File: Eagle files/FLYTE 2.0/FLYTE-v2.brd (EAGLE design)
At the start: 116 x 55 mm, 56 parts, among them U2 XBP9B-XCST-021, U3 ADS1115IDGSR, U4 H3LIS200DLTR, U5 BS170F, U6 W25Q32JVSSIQ, U7 BS170F

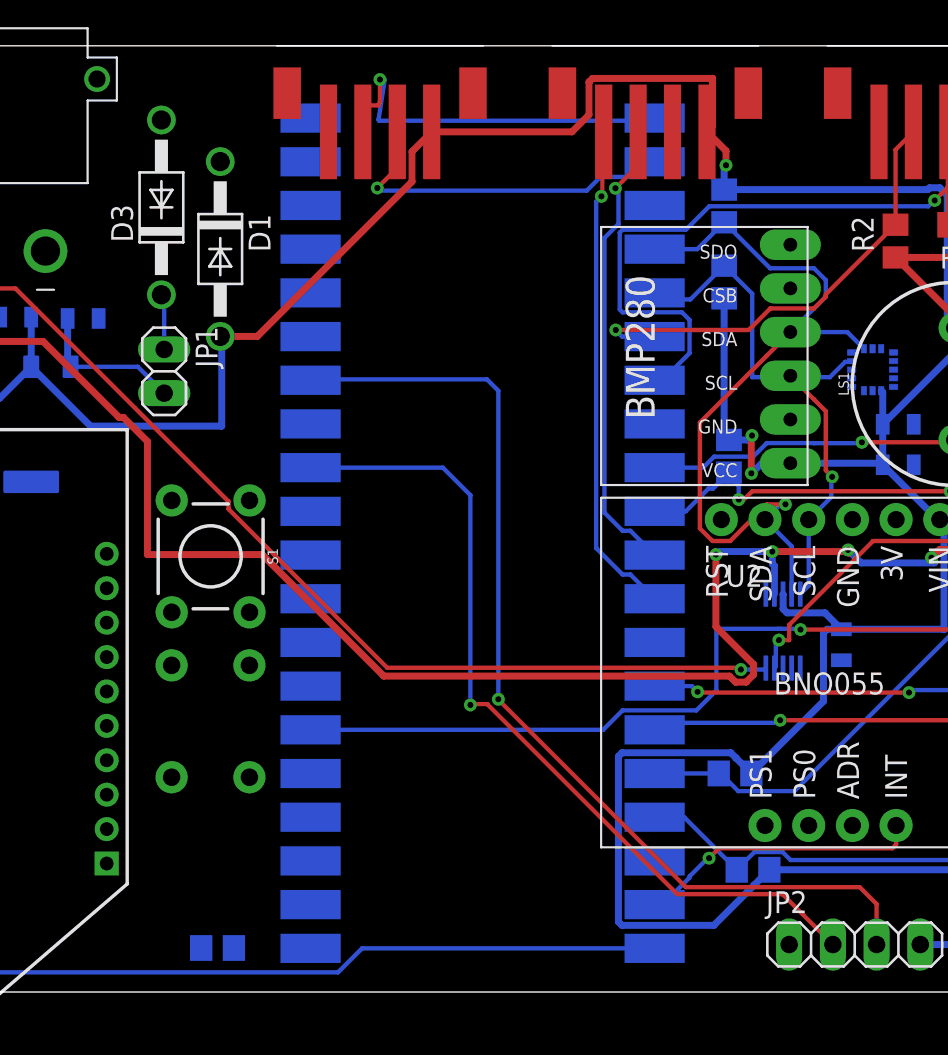
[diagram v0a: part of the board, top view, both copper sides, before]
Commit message: layout done. drc left to clear
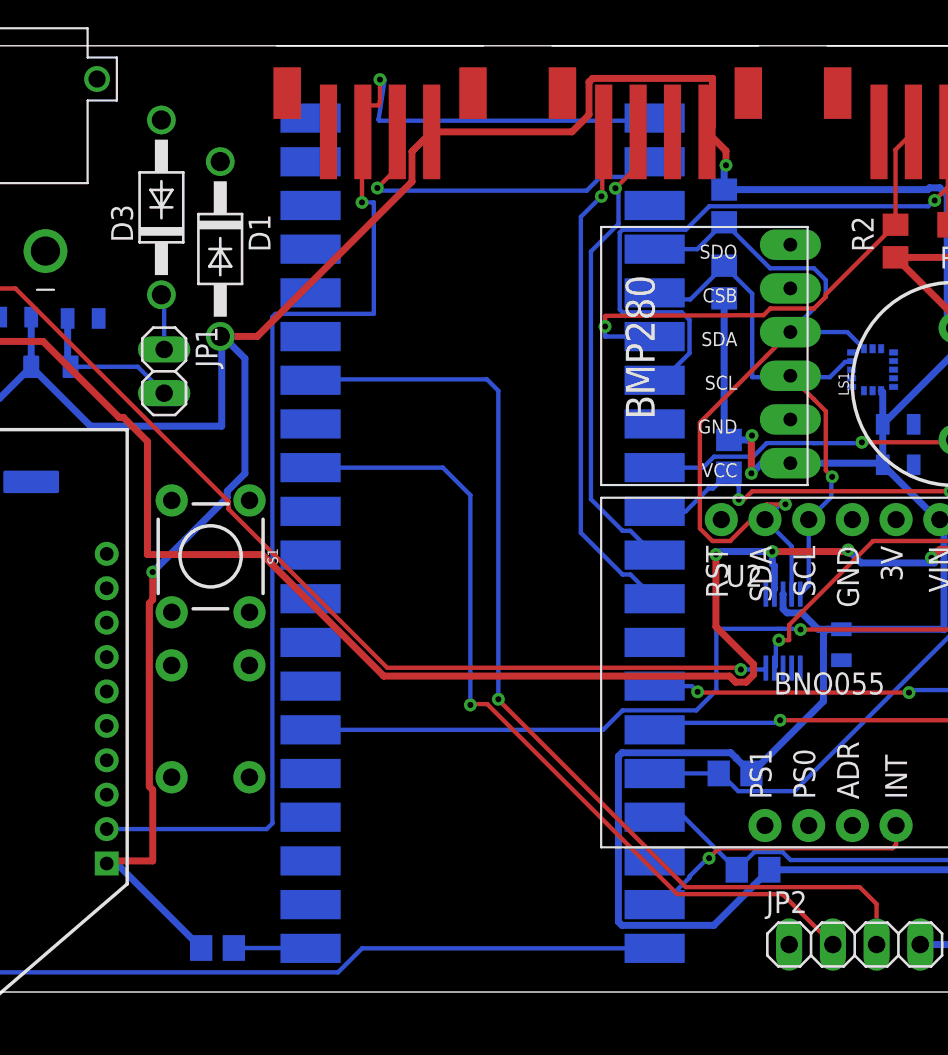
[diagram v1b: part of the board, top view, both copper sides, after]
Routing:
- net SER_TX: track 22.8 -> 79.4 mm, vias 1 -> 2
- net 3V3: track 266.3 -> 310.0 mm, vias 4 -> 5
- net MISO0: track 0.00 -> 4.47 mm
- net SDA0: track 27.2 -> 29.0 mm
- net RX: track 29.0 -> 29.7 mm
- net TX: track 27.3 -> 27.9 mm
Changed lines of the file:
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@@
 <wire x1="18" y1="50.73" x2="22.5998" y2="50.73" width="0.4064" layer="16"/>
 <wire x1="22.5998" y1="50.73" x2="30.4049" y2="42.9249" width="0.4064" layer="16"/>
-<wire x1="77.9224" y1="23.129" x2="77.9224" y2="24.7698" width="0.4064" layer="16"/>
 <via x="77.8002" y="25.6032" extent="1-16" drill="0.35"/>
 <wire x1="77.8002" y1="25.6032" x2="82.169" y2="25.6032" width="0.4064" layer="1"/>
@@
 <wire x1="98" y1="37.06175" x2="98" y2="50.73" width="0.4064" layer="1"/>
 <wire x1="94.059" y1="33.12075" x2="98" y2="37.06175" width="0.4064" layer="1"/>
-<wire x1="77.9224" y1="24.7698" x2="77.8002" y2="24.892" width="0.4064" layer="16"/>
+<wire x1="77.8002" y1="24.892" x2="77.9224" y2="24.7698" width="0.4064" layer="16"/>
 <wire x1="77.8002" y1="24.892" x2="77.8002" y2="25.6032" width="0.4064" layer="16"/>
 <wire x1="77.8002" y1="25.6032" x2="74.5236" y2="25.6032" width="0.4064" layer="16"/>
@@
 <wire x1="41.4782" y1="32.004" x2="41.4782" y2="25.4254" width="0.4064" layer="1"/>
 <wire x1="35.4076" y1="37.8206" x2="39.8272" y2="33.401" width="0.4064" layer="1"/>
+<wire x1="77.9224" y1="24.7698" x2="77.9224" y2="23.41926875" width="0.4064" layer="16"/>
+<wire x1="77.9224" y1="23.41926875" x2="77.918" y2="23.41486875" width="0.4064" layer="16"/>
+<wire x1="77.918" y1="23.41486875" x2="77.9224" y2="23.129" width="0" layer="19" extent="16-16"/>
 </signal>
 <signal name="SCL1">
@@
 <wire x1="84.9614" y1="42.7042" x2="88.347" y2="39.3186" width="0.4064" layer="1"/>
 <wire x1="88.347" y1="39.3186" x2="88.347" y2="38.5992" width="0.4064" layer="1"/>
-<wire x1="78.65560625" y1="22.0384" x2="78.4268" y2="22.26720625" width="0.4064" layer="16"/>
-<wire x1="81.8148" y1="21.0862" x2="80.8626" y2="22.0384" width="0.4064" layer="16"/>
-<wire x1="78.4268" y1="22.26720625" x2="78.4268" y2="23.1246" width="0.4064" layer="16"/>
-<wire x1="78.4268" y1="23.1246" x2="78.4224" y2="23.129" width="0.4064" layer="16"/>
-<wire x1="80.8626" y1="22.0384" x2="78.65560625" y2="22.0384" width="0.4064" layer="16"/>
 <wire x1="86.4" y1="2.76" x2="95.8764" y2="2.76" width="0.4064" layer="16"/>
 <wire x1="95.8764" y1="2.76" x2="96.98" y2="3.8636" width="0.4064" layer="16"/>
@@
 <wire x1="74.40109375" y1="3.8744" x2="69.06270625" y2="3.8744" width="0.4064" layer="16"/>
 <wire x1="68.8544" y1="4.08270625" x2="68.8544" y2="13.69729375" width="0.4064" layer="16"/>
+<wire x1="39.11" y1="7.47" x2="39.6884" y2="7.47" width="0.4064" layer="16"/>
+<wire x1="39.6884" y1="7.47" x2="44.6008" y2="2.5576" width="0.4064" layer="16"/>
+<wire x1="39.11" y1="7.47" x2="39.26" y2="7.62" width="0.4064" layer="1"/>
+<wire x1="39.26" y1="7.62" x2="41.783" y2="7.62" width="0.4064" layer="1"/>
+<wire x1="41.783" y1="7.62" x2="41.783" y2="11.753425" width="0.4064" layer="1"/>
+<wire x1="41.783" y1="11.753425" x2="41.5874" y2="11.949025" width="0.4064" layer="1"/>
+<wire x1="41.5874" y1="11.949025" x2="41.5874" y2="22.602375" width="0.4064" layer="1"/>
+<wire x1="41.5874" y1="22.602375" x2="41.783" y2="22.797975" width="0.4064" layer="1"/>
+<via x="41.783" y="24.4094" extent="1-16" drill="0.35"/>
+<wire x1="41.783" y1="24.4094" x2="46.115" y2="28.7414" width="0.4064" layer="16"/>
+<wire x1="46.115" y1="28.7414" x2="46.115" y2="29.111175" width="0.4064" layer="16"/>
+<wire x1="47.1424" y1="30.138575" x2="47.1424" y2="36.83" width="0.4064" layer="16"/>
+<wire x1="46.115" y1="29.111175" x2="47.1424" y2="30.138575" width="0.4064" layer="16"/>
+<wire x1="47.1424" y1="36.83" x2="45.9486" y2="38.0238" width="0.4064" layer="16"/>
+<wire x1="45.9486" y1="38.0238" x2="45.7962" y2="38.0238" width="0.4064" layer="16"/>
+<wire x1="41.783" y1="22.797975" x2="41.783" y2="24.4094" width="0.4064" layer="1"/>
+<wire x1="80.4652" y1="21.0862" x2="81.8148" y2="21.0862" width="0.4064" layer="16"/>
+<wire x1="78.4224" y1="23.129" x2="78.4268" y2="23.1246" width="0.4064" layer="16"/>
+<wire x1="78.4268" y1="23.1246" x2="78.4268" y2="22.26720625" width="0.4064" layer="16"/>
+<wire x1="78.4268" y1="22.26720625" x2="78.65560625" y2="22.0384" width="0.4064" layer="16"/>
+<wire x1="79.513" y1="22.0384" x2="80.4652" y2="21.0862" width="0.4064" layer="16"/>
+<wire x1="78.65560625" y1="22.0384" x2="79.513" y2="22.0384" width="0.4064" layer="16"/>
 <wire x1="83.6266" y1="34.955" x2="82.4066" y2="35.175" width="0" layer="19" extent="16-16"/>
 <wire x1="84.1266" y1="34.955" x2="83.6266" y2="34.955" width="0" layer="19" extent="16-16"/>
 <wire x1="77.4224" y1="23.129" x2="78.4224" y2="23.129" width="0" layer="19" extent="16-16"/>
-<wire x1="39.11" y1="7.47" x2="34.72" y2="36.345" width="0" layer="19" extent="16-16"/>
-<wire x1="44.6008" y1="2.5576" x2="39.11" y2="7.47" width="0" layer="19" extent="16-16"/>
 </signal>
 <signal name="TX">
@@
 <wire x1="70.96" y1="25.4" x2="69.5494" y2="26.8106" width="0.254" layer="16"/>
 <wire x1="69.5494" y1="26.8106" x2="69.09426875" y2="26.8106" width="0.254" layer="16"/>
-<wire x1="68.0416" y1="43.83146875" x2="68.8594" y2="44.64926875" width="0.254" layer="16"/>
+<wire x1="67.2542" y1="43.04406875" x2="68.8594" y2="44.64926875" width="0.254" layer="16"/>
 <wire x1="68.8594" y1="44.64926875" x2="68.8594" y2="46.8122" width="0.254" layer="16"/>
-<wire x1="69.09426875" y1="26.8106" x2="68.0416" y2="27.86326875" width="0.254" layer="16"/>
-<wire x1="68.0416" y1="27.86326875" x2="68.0416" y2="43.83146875" width="0.254" layer="16"/>
+<wire x1="69.09426875" y1="26.8106" x2="67.2542" y2="28.65066875" width="0.254" layer="16"/>
+<wire x1="67.2542" y1="28.65066875" x2="67.2542" y2="43.04406875" width="0.254" layer="16"/>
 <wire x1="68.8594" y1="46.8122" x2="68.7722" y2="46.8122" width="0.254" layer="16"/>
 <wire x1="68.7722" y1="46.8122" x2="68.6794" y2="46.7194" width="0.254" layer="16"/>
@@
 <wire x1="70.96" y1="22.86" x2="69.5494" y2="24.2706" width="0.254" layer="16"/>
 <wire x1="69.5494" y1="24.2706" x2="69.09426875" y2="24.2706" width="0.254" layer="16"/>
-<wire x1="69.09426875" y1="24.2706" x2="67.55968125" y2="25.8051875" width="0.254" layer="16"/>
-<wire x1="67.55968125" y1="45.94428125" x2="67.55968125" y2="25.8051875" width="0.254" layer="16"/>
-<wire x1="67.55968125" y1="45.94428125" x2="67.86448125" y2="46.24908125" width="0.254" layer="16"/>
+<wire x1="69.09426875" y1="24.2706" x2="66.67068125" y2="26.6941875" width="0.254" layer="16"/>
+<wire x1="66.67068125" y1="45.05528125" x2="66.67068125" y2="26.6941875" width="0.254" layer="16"/>
+<wire x1="66.67068125" y1="45.05528125" x2="67.86448125" y2="46.24908125" width="0.254" layer="16"/>
 <via x="67.86448125" y="46.24908125" extent="1-16" drill="0.35"/>
 <wire x1="67.86448125" y1="46.24908125" x2="67.9196" y2="46.3042" width="0.254" layer="1"/>
@@
 <contactref element="U1" pad="P$21"/>
 <contactref element="R16" pad="1"/>
-<wire x1="46.5008" y1="2.5576" x2="50.96" y2="2.54" width="0" layer="19" extent="16-16"/>
+<wire x1="46.5008" y1="2.5576" x2="50.9424" y2="2.5576" width="0.254" layer="16"/>
+<wire x1="50.9424" y1="2.5576" x2="50.96" y2="2.54" width="0.254" layer="16"/>
 </signal>
 <signal name="CS_FLASH">
@@
 <wire x1="86" y1="50" x2="84.9614" y2="48.9614" width="0.254" layer="1"/>
 <wire x1="84.9614" y1="48.9614" x2="84.9614" y2="44.6042" width="0.254" layer="1"/>
-<wire x1="70.96" y1="38.1" x2="69.0626" y2="38.1" width="0.254" layer="16"/>
-<wire x1="69.0626" y1="38.1" x2="68.6816" y2="38.481" width="0.254" layer="16"/>
-<wire x1="68.6816" y1="38.481" x2="68.6992" y2="38.481" width="0.254" layer="16"/>
-<via x="68.6992" y="38.481" extent="1-16" drill="0.35"/>
+<wire x1="70.96" y1="38.1" x2="68.0798" y2="38.1" width="0.254" layer="16"/>
+<wire x1="68.0798" y1="38.1" x2="68.0798" y2="38.6842" width="0.254" layer="16"/>
+<via x="68.0798" y="38.6842" extent="1-16" drill="0.35"/>
 <wire x1="80.22296875" y1="39.7316" x2="80.9074" y2="40.41603125" width="0.254" layer="1"/>
 <wire x1="80.9074" y1="40.41603125" x2="80.9074" y2="40.5502" width="0.254" layer="1"/>
 <wire x1="80.9074" y1="40.5502" x2="84.9614" y2="44.6042" width="0.254" layer="1"/>
-<wire x1="68.6992" y1="38.481" x2="76.42963125" y2="38.481" width="0.254" layer="1"/>
-<wire x1="76.42963125" y1="38.481" x2="77.68023125" y2="39.7316" width="0.254" layer="1"/>
+<wire x1="68.11175" y1="39.30596875" x2="68.0798" y2="39.27401875" width="0.254" layer="1"/>
+<wire x1="68.0798" y1="38.6842" x2="68.0798" y2="39.27401875" width="0.254" layer="1"/>
+<wire x1="77.28936875" y1="39.3407375" x2="68.11175" y2="39.30596875" width="0.254" layer="1"/>
+<wire x1="77.28936875" y1="39.3407375" x2="77.68023125" y2="39.7316" width="0.254" layer="1"/>
 <wire x1="77.68023125" y1="39.7316" x2="80.22296875" y2="39.7316" width="0.254" layer="1"/>
 </signal>
@@
 <wire x1="54.991" y1="51.774284375" x2="54.915253125" y2="51.5366" width="0.254" layer="1"/>
 <wire x1="54.915253125" y1="51.5366" x2="54" y2="51.5366" width="0.254" layer="1"/>
-<wire x1="54" y1="51.5366" x2="54" y2="50" width="0.254" layer="1"/>
+<wire x1="54" y1="51.5366" x2="54" y2="50.1904" width="0.254" layer="1"/>
 <contactref element="U2" pad="2"/>
-<wire x1="39.11" y1="9.47" x2="54" y2="50" width="0" layer="19" extent="1-1"/>
+<wire x1="54" y1="50.1904" x2="54" y2="50" width="0.254" layer="1"/>
+<wire x1="39.11" y1="9.47" x2="48.4082" y2="9.47" width="0.254" layer="16"/>
+<wire x1="48.7426" y1="9.8044" x2="48.7426" y2="39.243" width="0.254" layer="16"/>
+<wire x1="48.7426" y1="39.243" x2="48.9204" y2="39.4208" width="0.254" layer="16"/>
+<wire x1="48.9204" y1="39.4208" x2="54.6354" y2="39.4208" width="0.254" layer="16"/>
+<wire x1="54.6354" y1="39.4208" x2="54.6354" y2="45.8978" width="0.254" layer="16"/>
+<wire x1="54.6354" y1="45.8978" x2="53.9496" y2="45.8978" width="0.254" layer="16"/>
+<via x="53.9496" y="45.8978" extent="1-16" drill="0.35"/>
+<wire x1="53.9496" y1="45.8978" x2="53.9496" y2="50.14" width="0.254" layer="1"/>
+<wire x1="53.9496" y1="50.14" x2="54" y2="50.1904" width="0.254" layer="1"/>
+<wire x1="48.4082" y1="9.47" x2="48.7426" y2="9.8044" width="0.254" layer="16"/>
 </signal>
 <signal name="SER_RX">

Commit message: updated layout
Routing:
- net GND: track 0.00 -> 125.5 mm, vias 0 -> 11
- net N$3: track 0.00 -> 23.1 mm, vias 0 -> 1
- net N$8: track 0.00 -> 9.52 mm, vias 0 -> 1
- net N$17: track 0.00 -> 8.72 mm
- net N$1: track 0.00 -> 5.25 mm
- net 3V3: track 310.0 -> 314.7 mm
- net N$5: track 10.4 -> 13.8 mm
- net BNO_INT: track 16.6 -> 19.3 mm
- net N$12: track 7.01 -> 9.18 mm

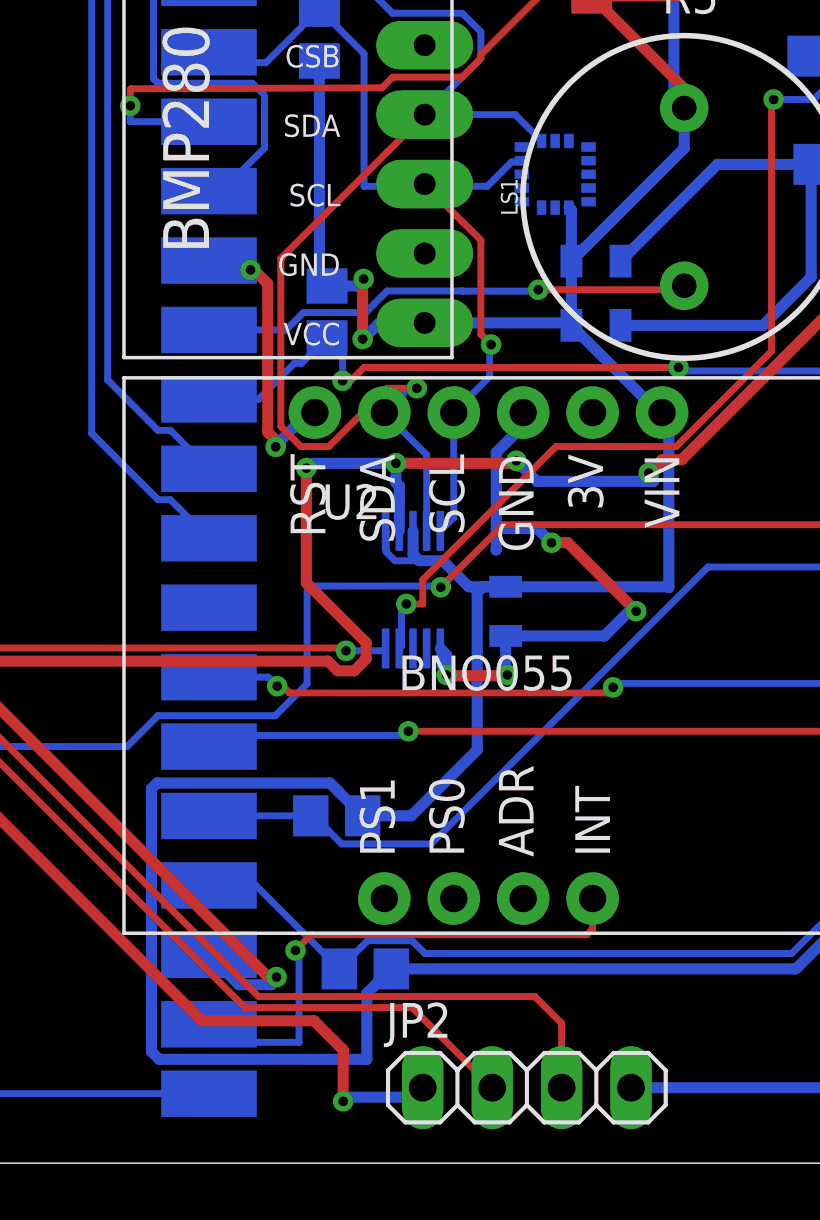
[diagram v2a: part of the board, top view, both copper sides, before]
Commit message: updated layout
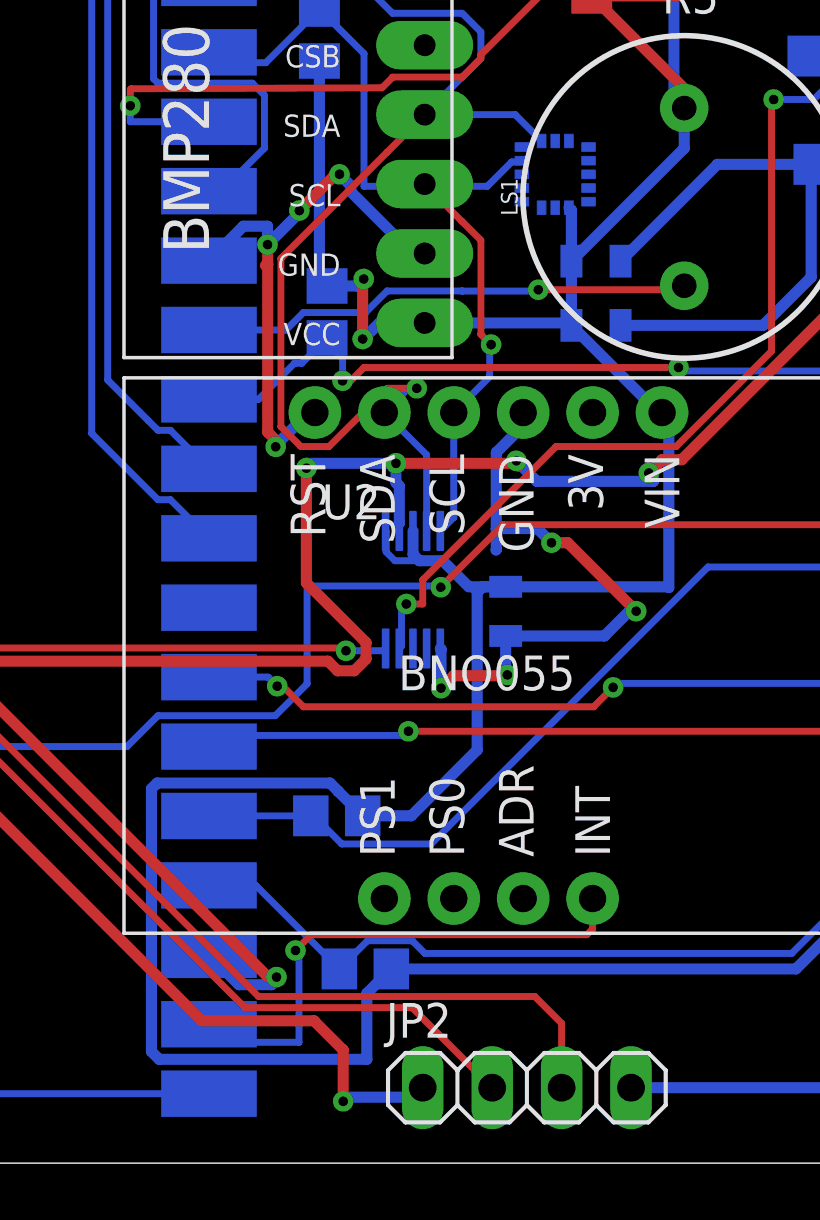
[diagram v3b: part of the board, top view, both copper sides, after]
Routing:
- net GND: track 125.5 -> 136.9 mm, vias 11 -> 13

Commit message: layout done
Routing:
- net GND: track 136.9 -> 151.1 mm, vias 13 -> 17
- net 3V3: track 314.7 -> 317.4 mm

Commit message: .
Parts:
- moved U2 4.67 mm to (28.1, 11.5)
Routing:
- net DROGUE: track 101.7 -> 88.5 mm, vias 0 -> 2
- net 3V3: track 317.4 -> 313.7 mm
- net AIR_DATA: track 60.4 -> 59.2 mm
- net GND: track 151.1 -> 152.0 mm
- net VCC: track 139.8 -> 138.9 mm
- net MAIN: track 65.7 -> 65.1 mm
- net SER_TX: track 79.4 -> 80.0 mm
- net MISO1: track 41.7 -> 42.3 mm
- net SCL1: track 34.0 -> 33.5 mm

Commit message: Finish layout for v2
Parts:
- added LED1, LED2: (no value), led:CHIPLED_1206
- added R13: (no value), rcl:R0805
- R16: value 100K ohm -> (none)
- moved S1 13.7 mm to (45.2, 11.6)
- moved R16 13.5 mm to (56.7, 10.2), flipped to the top
- moved S2 4.98 mm to (45.2, 20.7), turned to 90 degrees
- moved JP2 2.06 mm to (83.9, 4.39)
- moved U6 1.27 mm to (106.4, 25.1)
- moved R14 0.88 mm to (75.9, 6.71), turned to 90 degrees
- moved R17 0.67 mm to (75.9, 13.3), turned to 270 degrees
- moved R1 0.36 mm to (21.0, 38.1), turned to 270 degrees
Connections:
- removed net MISO0: R16.1, U1.P$21
- removed net MOSI0: U1.P$25
- removed net SEX_RX: U2.3
- new net LED1: R13.1, U1.P$25
- new net LED2: R16.1, U1.P$24
- new net N$14: LED1.C, R13.2
- new net N$15: LED2.C, R16.2
- net 3V3: now also LED1.A, LED2.A; no longer R16.2
- net AIR_DATA: now also U1.P$21; no longer U1.P$34
- net AIR_SCK: now also U1.P$22; no longer U1.P$32
- net CTS: now also U1.P$32
- net DROGUE: now also U1.P$34; no longer U1.P$20
- net N$3: now also U1.P$31; no longer U1.P$29
- net SER_RX: now also U2.3
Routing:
- net GND: track 152.0 -> 85.8 mm, vias 17 -> 13
- net SER_RX: track 20.8 -> 70.6 mm, vias 1 -> 2
- net DROGUE: track 88.5 -> 40.4 mm, vias 2 -> 0
- net CTS: track 0.00 -> 48.0 mm
- net 3V3: track 313.7 -> 343.0 mm
- net AIR_DATA: track 59.2 -> 35.5 mm
- net VCC: track 138.9 -> 121.6 mm, vias 5 -> 4
- net AIR_SCK: track 49.0 -> 33.6 mm
- net SCL0: track 39.0 -> 26.6 mm
- net SDA1: track 46.8 -> 35.6 mm, vias 1 -> 0
- net N$8: track 9.52 -> 18.4 mm
- net SDA0: track 29.4 -> 22.5 mm
- net LED2: track 0.00 -> 4.82 mm, vias 0 -> 1
- net LED1: track 0.00 -> 4.81 mm, vias 0 -> 1
- net SER_TX: track 80.0 -> 84.4 mm, vias 2 -> 3
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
